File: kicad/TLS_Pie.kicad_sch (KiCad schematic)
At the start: 23 parts, among them M1 stepper + 50:1, U1 DS3231 breakout, U10 fan 5 V, U11 INA226 -- NOT FITTED, U12 BCD5A -> 16.8 V / 1.5 A (17.0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, U3 LM2596S-ADJ -> 5.1 V, U4 Big Easy Driver, U7 VLP-16 interface box, U8 Velodyne VLP-16

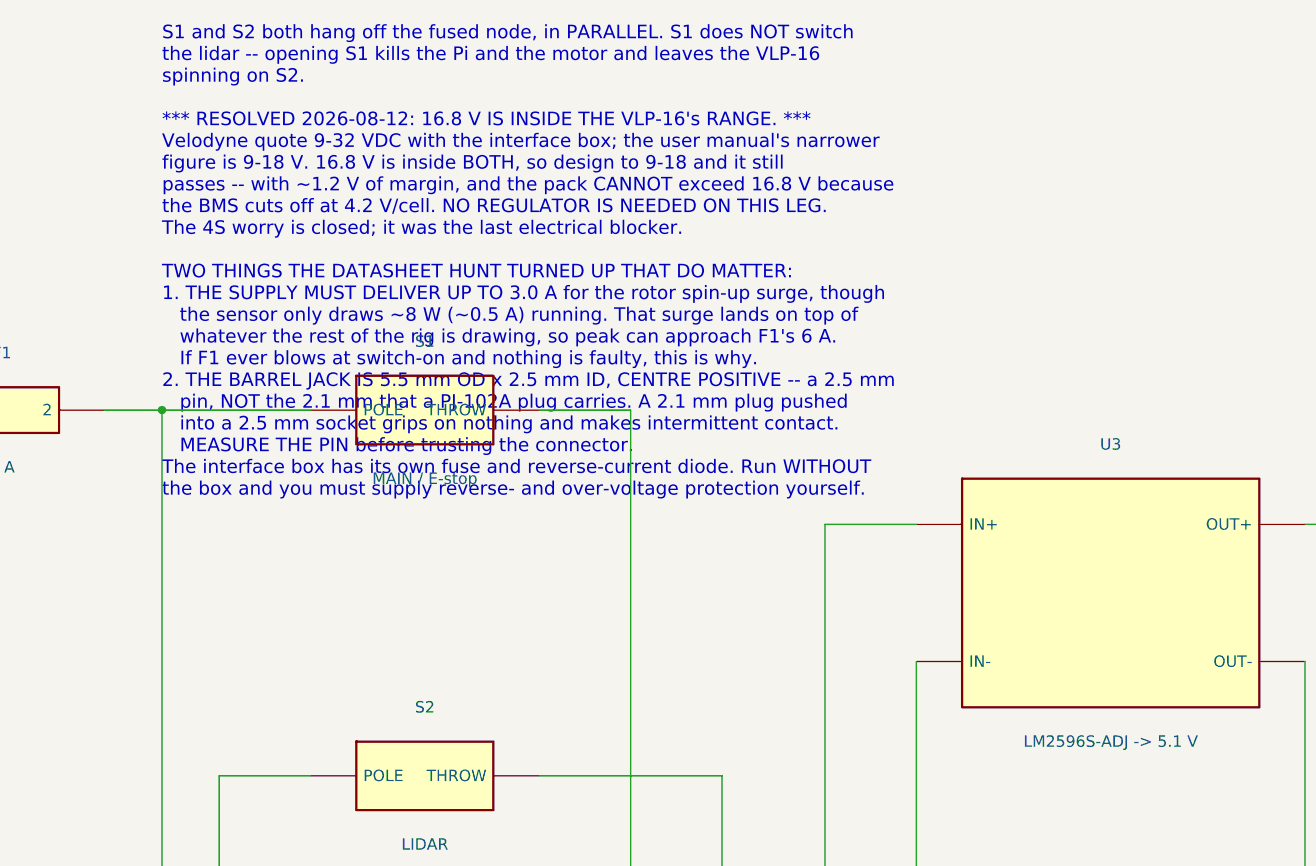
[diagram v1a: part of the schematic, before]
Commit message: No separate E-stop: S1 is the stop, and the record now says so
A deliberate call and a reasonable one for a 16.8 V ~50 W bench rig.  The
sheet had been calling S1 the E-stop, which it is not, and had been carrying a
DC-arc warning out of proportion to 16.8 V into a mostly capacitive load.
Both corrected rather than left to nag.

Two things do follow from the decision and are now written down:

  * S1 becomes safety-relevant by POSITION.  It has to be reachable without
    reaching over the moving head, and which way is OFF has to be obvious to
    someone who is not thinking clearly.  A latched toggle gives none of the
    affordances a mushroom head does, so the mounting has to.
  * S1 does not stop the lidar.  S1 and S2 hang off the fused node in
    parallel, so opening S1 kills the Pi and the motor -- which is the actual
    hazard, the head on a 50:1 gearbox -- and leaves the VLP-16 spinning on
    S2.  Everything off means both switches.

The DC rating is now framed as one look rather than an open blocker: >=20 VDC
at >=5 A is plenty.

Verified: 2186 validator checks 0 failed; KiCad ERC 0 violations.

Co-Authored-By: Claude Opus 5 <noreply@anthropic.com>
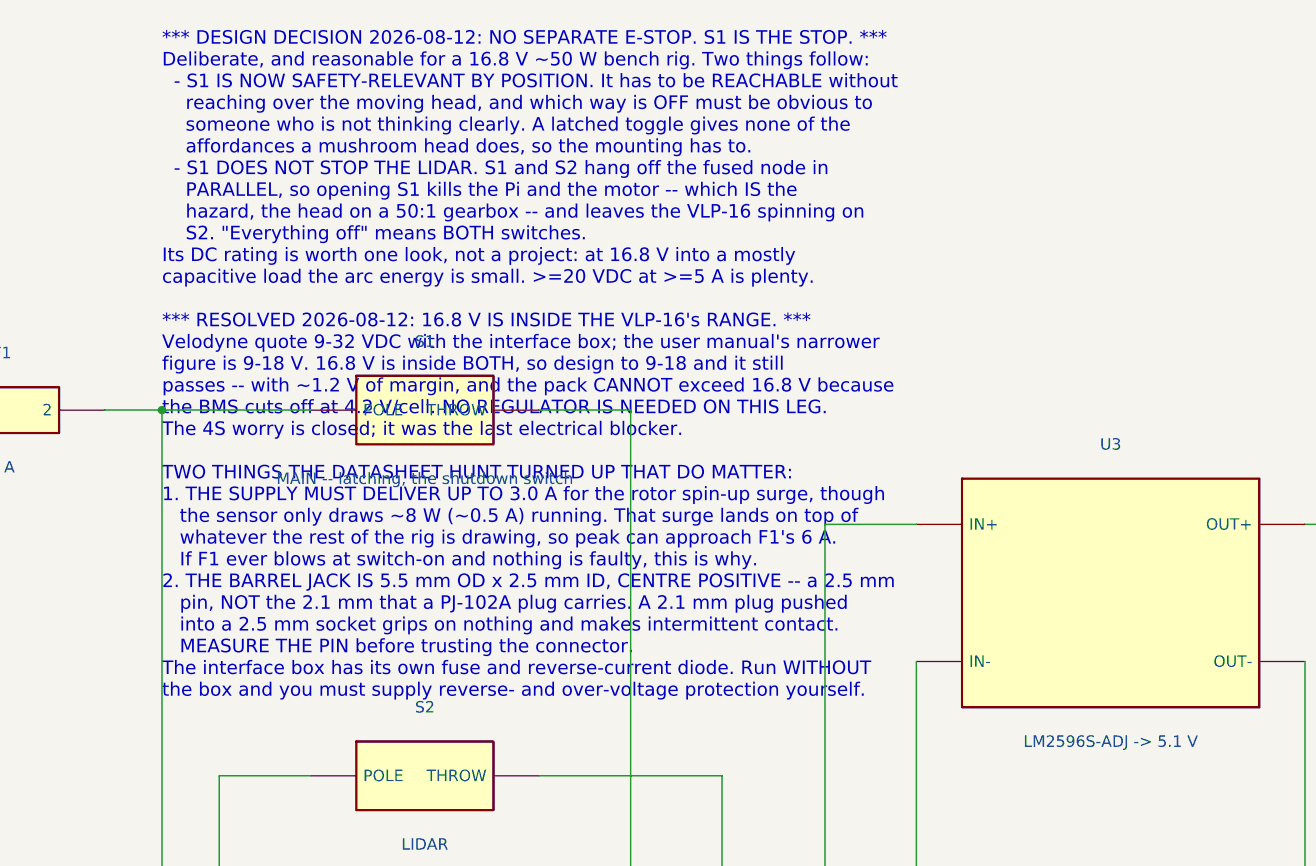
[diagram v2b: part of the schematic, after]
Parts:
- S1: value MAIN / E-stop -> MAIN -- latching, the shutdown switch
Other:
- note added: "*** DESIGN DECISION 2026-08-12: NO SEPARATE E-STOP. S1 IS THE STOP. *** Deliberate, and reasonable for a 16.8 V ~50 W bench rig. Two things follow: - S1 IS NOW SAFETY-RELEVANT BY POSITION. It has to be REACHABLE without reaching over the moving head, and which way is OFF must be obvious to someone who is not thinking clearly. A latched toggle gives none of the affordances a mushroom head does, so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"
- note removed: "S1 and S2 both hang off the fused node, in PARALLEL. S1 does NOT switch the lidar -- opening S1 kills the Pi and the motor and leaves the VLP-16 spinning on S2. *** RESOLVED 2026-08-12: 16.8 V IS INSIDE THE VLP-16's RANGE. *** Velodyne quote 9-32 VDC with the interface box; the user manual's narrower figure is 9-18 V. 16.8 V is inside BOTH, so design to 9-18 and it still passes -- with ~1.2 V of 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"
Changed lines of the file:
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@@
       (effects (font (size 1.27 1.27)))
     )
-    (property "Value" "MAIN / E-stop"
+    (property "Value" "MAIN -- latching, the shutdown switch"
       (at 226.06 66.04 0)
       (effects (font (size 1.27 1.27)))
@@
       (effects (font (size 1.27 1.27)))
     )
-    (property "Description" "Power switch -- check the DC rating, a DC arc does not self-extinguish"
+    (property "Description" "Latching power switch. DC arcs do not self-extinguish, but at 16.8 V and ~3 A into a mostly capacitive load that risk is small -- check the marking once and move on. Anything rated >=20 VDC at >=5 A is fine"
       (at 226.06 58.42 0)
       (hide yes)
@@
       (effects (font (size 1.27 1.27)))
     )
-    (property "Description" "Power switch -- check the DC rating, a DC arc does not self-extinguish"
+    (property "Description" "Latching power switch. DC arcs do not self-extinguish, but at 16.8 V and ~3 A into a mostly capacitive load that risk is small -- check the marking once and move on. Anything rated >=20 VDC at >=5 A is fine"
       (at 226.06 99.06 0)
       (hide yes)
@@
       (effects (font (size 1.27 1.27)))
     )
-    (property "Description" "Power switch -- check the DC rating, a DC arc does not self-extinguish"
+    (property "Description" "Latching power switch. DC arcs do not self-extinguish, but at 16.8 V and ~3 A into a mostly capacitive load that risk is small -- check the marking once and move on. Anything rated >=20 VDC at >=5 A is fine"
       (at 537.21 30.48 0)
       (hide yes)
@@
   (wire (pts (xy 481.33 99.06) (xy 524.51 99.06)) (stroke (width 0) (type default)))
   (wire (pts (xy 524.51 99.06) (xy 524.51 86.36)) (stroke (width 0) (type default)))
-  (text "S1 and S2 both hang off the fused node, in PARALLEL. S1 does NOT switch\nthe lidar -- opening S1 kills the Pi and the motor and leaves the VLP-16\nspinning on S2.\n\n*** RESOLVED 2026-08-12: 16.8 V IS INSIDE THE VLP-16's RANGE. ***\nVelodyne quote 9-32 VDC with the interface box; the user manual's narrower\nfigure is 9-18 V. 16.8 V is inside BOTH, so design to 9-18 and it still\npasses -- with ~1.2 V of margin, and the pack CANNOT exceed 16.8 V because\nthe BMS cuts off at 4.2 V/cell. NO REGULATOR IS NEEDED ON THIS LEG.\nThe 4S worry is closed; it was the last electrical blocker.\n\nTWO THINGS THE DATASHEET HUNT TURNED UP THAT DO MATTER:\n1. THE SUPPLY MUST DELIVER UP TO 3.0 A for the rotor spin-up surge, though\n   the sensor only draws ~8 W (~0.5 A) running. That surge lands on top of\n   whatever the rest of the rig is drawing, so peak can approach F1's 6 A.\n   If F1 ever blows at switch-on and nothing is faulty, this is why.\n2. THE BARREL JACK IS 5.5 mm OD x 2.5 mm ID, CENTRE POSITIVE -- a 2.5 mm\n   pin, NOT the 2.1 mm that a PJ-102A plug carries. A 2.1 mm plug pushed\n   into a 2.5 mm socket grips on nothing and makes intermittent contact.\n   MEASURE THE PIN before trusting the connector.\nThe interface box has its own fuse and reverse-current diode. Run WITHOUT\nthe box and you must supply reverse- and over-voltage protection yourself." (exclude_from_sim yes) (at 196.85 42.015 0) (effects (font (size 1.5 1.5)) (justify left)))
+  (text "*** DESIGN DECISION 2026-08-12: NO SEPARATE E-STOP. S1 IS THE STOP. ***\nDeliberate, and reasonable for a 16.8 V ~50 W bench rig. Two things follow:\n  - S1 IS NOW SAFETY-RELEVANT BY POSITION. It has to be REACHABLE without\n    reaching over the moving head, and which way is OFF must be obvious to\n    someone who is not thinking clearly. A latched toggle gives none of the\n    affordances a mushroom head does, so the mounting has to.\n  - S1 DOES NOT STOP THE LIDAR. S1 and S2 hang off the fused node in\n    PARALLEL, so opening S1 kills the Pi and the motor -- which IS the\n    hazard, the head on a 50:1 gearbox -- and leaves the VLP-16 spinning on\n    S2. \"Everything off\" means BOTH switches.\nIts DC rating is worth one look, not a project: at 16.8 V into a mostly\ncapacitive load the arc energy is small. >=20 VDC at >=5 A is plenty.\n\n*** RESOLVED 2026-08-12: 16.8 V IS INSIDE THE VLP-16's RANGE. ***\nVelodyne quote 9-32 VDC with the interface box; the user manual's narrower\nfigure is 9-18 V. 16.8 V is inside BOTH, so design to 9-18 and it still\npasses -- with ~1.2 V of margin, and the pack CANNOT exceed 16.8 V because\nthe BMS cuts off at 4.2 V/cell. NO REGULATOR IS NEEDED ON THIS LEG.\nThe 4S worry is closed; it was the last electrical blocker.\n\nTWO THINGS THE DATASHEET HUNT TURNED UP THAT DO MATTER:\n1. THE SUPPLY MUST DELIVER UP TO 3.0 A for the rotor spin-up surge, though\n   the sensor only draws ~8 W (~0.5 A) running. That surge lands on top of\n   whatever the rest of the rig is drawing, so peak can approach F1's 6 A.\n   If F1 ever blows at switch-on and nothing is faulty, this is why.\n2. THE BARREL JACK IS 5.5 mm OD x 2.5 mm ID, CENTRE POSITIVE -- a 2.5 mm\n   pin, NOT the 2.1 mm that a PJ-102A plug carries. A 2.1 mm plug pushed\n   into a 2.5 mm socket grips on nothing and makes intermittent contact.\n   MEASURE THE PIN before trusting the connector.\nThe interface box has its own fuse and reverse-current diode. Run WITHOUT\nthe box and you must supply reverse- and over-voltage protection yourself." (exclude_from_sim yes) (at 196.85 53.49 0) (effects (font (size 1.5 1.5)) (justify left)))
   (text "CONNECT THE TAPS IN THIS ORDER:  0V  4.2V  8.4V  12.6V  16.8V\nThe board names its pads by voltage, and those are FULL-CHARGE values --\nNOT what a flat pack measures. Against 0V at the measured 12.24 V total you\nshould read roughly:   0 / 3.06 / 6.12 / 9.18 / 12.24 V.\nWHAT MATTERS IS THE ORDER, evenly spaced and ascending. Meter every tap on\nthe free connector BEFORE plugging it in.\nThe protection ICs are powered from the taps. Out of order, one stage sees\nmost of the pack across single-cell inputs and dies silently -- leaving a\nboard that looks fine and protects nothing. Solder all five to the pack\nFIRST, meter the free connector, and only then plug it in.\n\n4.2V/8.4V/12.6V carry milliamps -- 22-24 AWG.  16.8V (B+) and 0V (B-) carry\nthe FULL pack current -- run those two THICK. Check the 16.8V lead: it is\nthe one that looks like a balance wire and is not.\n\n*** PAD ADJACENCY ON THE REAL BOARD -- ONE SLIP IS A FIRE ***\nRight edge, top to bottom:  16.8V | (+) | (-) | 4.2V.\n  (+) beside 16.8V   -- a bridge here is HARMLESS. They are the same copper:\n                        the ten FETs are all in the NEGATIVE leg, so the\n                        positive is never switched. MEASURED 0 ohms on the\n                        board 2026-08-11 -- this is verified, not inferred.\n  (-) beside 4.2V    -- a bridge here is the WORST SHORT ON THE BOARD. (-) is\n                        pack negative through the FETs and 4.2V is the top of\n                        group 1, so a stray strand puts a DEAD SHORT ACROSS\n                        THREE PARALLEL CELLS. No fuse is in that path and\n                        nothing protects it. Sleeve it, inspect it, and work\n                        that corner one lead at a time.\nLeave the CD and FD test pads alone." (exclude_from_sim yes) (at 34.29 160.155 0) (effects (font (size 1.5 1.5)) (justify left)))
   (text "PANEL METER PM1 -- and it changes the ground topology, so read this.\n\nITS THICK PAIR IS THE SHUNT, AND THE SHUNT IS IN THE NEGATIVE LEG. So it\ngoes in the RETURN, between the rig's ground and P- -- NOT in the +VBATT\nrail where U11 goes. GND and P- are now separate nodes joined ONLY through\nPM1. They cross twice on this sheet with no junction dot and are NOT\nconnected there. Bridge them anywhere and you short out the shunt: the\nmeter reads 0.00 A for ever and nothing warns you.\n\n*** VERIFY THE SHUNT LEG BEFORE SOLDERING ***\nMeter resistance thin-black to thick-black. NEAR ZERO = negative-leg shunt\nand this drawing is right. If instead thin-RED reads near zero to a thick\nlead, the shunt is in the POSITIVE leg -- then it belongs where U11 is, in\nthe +VBATT rail, and this corner of the sheet must be redrawn.\nThe two thick leads should read a fraction of an ohm to each other: that\nIS the shunt.\n\nTHIN BLACK GOES TO THE SAME SIDE AS THICK BLACK (P-). On most of these the\ntwo blacks are common inside the meter, so putting the thin one on the rig\nside of the shunt bridges it -- the same silent zero-amps failure.\n\nSUPPLY FROM +VSW1, NOT +VBATT. These meters draw ~20 mA continuously. On\n+VBATT that is ~0.5 Ah/day and would flatten this ~9 Ah pack in about three\nweeks of standing -- which is how it got flat the first time. On +VSW1 it\ndies with S1. VSENSE still reads TRUE PACK VOLTS because it taps +VBATT\nupstream of the switch, and it draws only microamps through its divider.\n\nReads 0.00 A while charging with S1 and S2 open. Correct: the charge return\nis on the pack side of the shunt, so charge current never crosses it.\nIts two thick leads carry the WHOLE rig's return -- mount PM1 at the BMS and\nkeep them short and heavy. The 6 A fuse is what keeps this inside its 10 A." (exclude_from_sim yes) (at 196.85 241.43 0) (effects (font (size 1.3 1.3)) (justify left)))
